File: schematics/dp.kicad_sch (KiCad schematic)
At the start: 27 parts, among them J9 DisplayPort_Molex_472720001, U28 74AVC4T245_UQFN, U29 FIN1019MTC, U30 TPD4E05U06QDQARQ1, U31 824012823

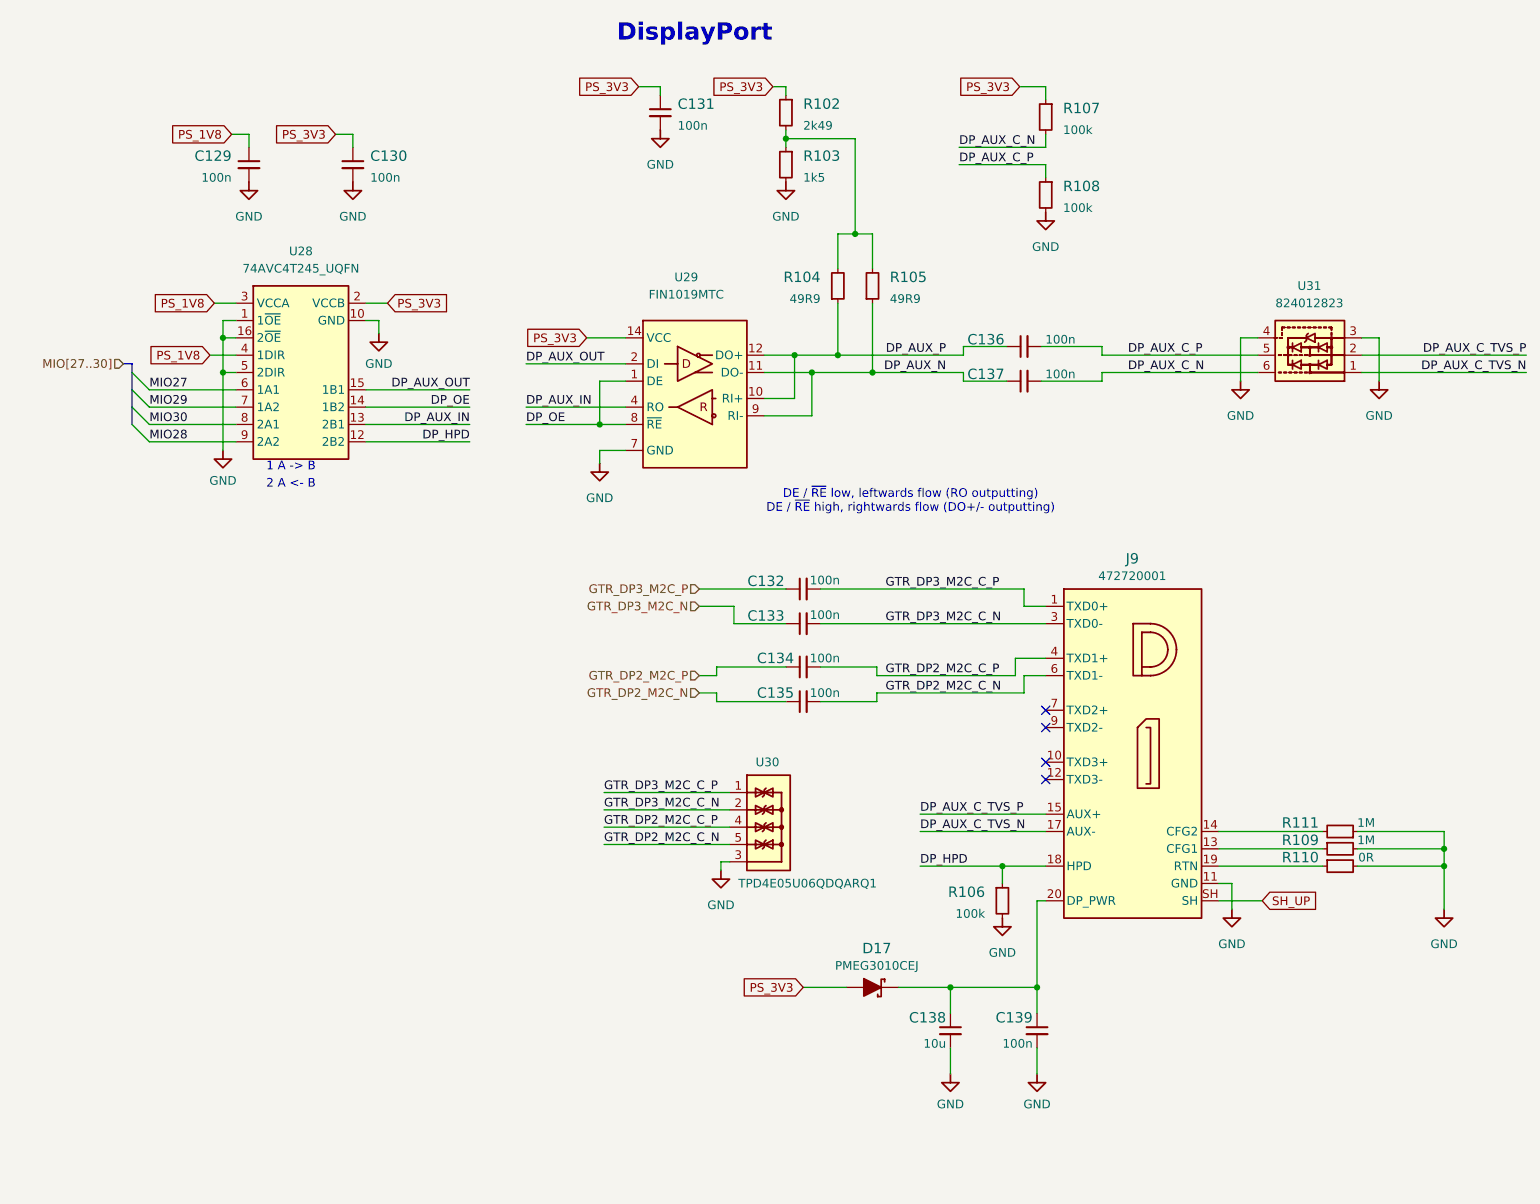
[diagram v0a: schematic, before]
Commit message: Voltage converter added
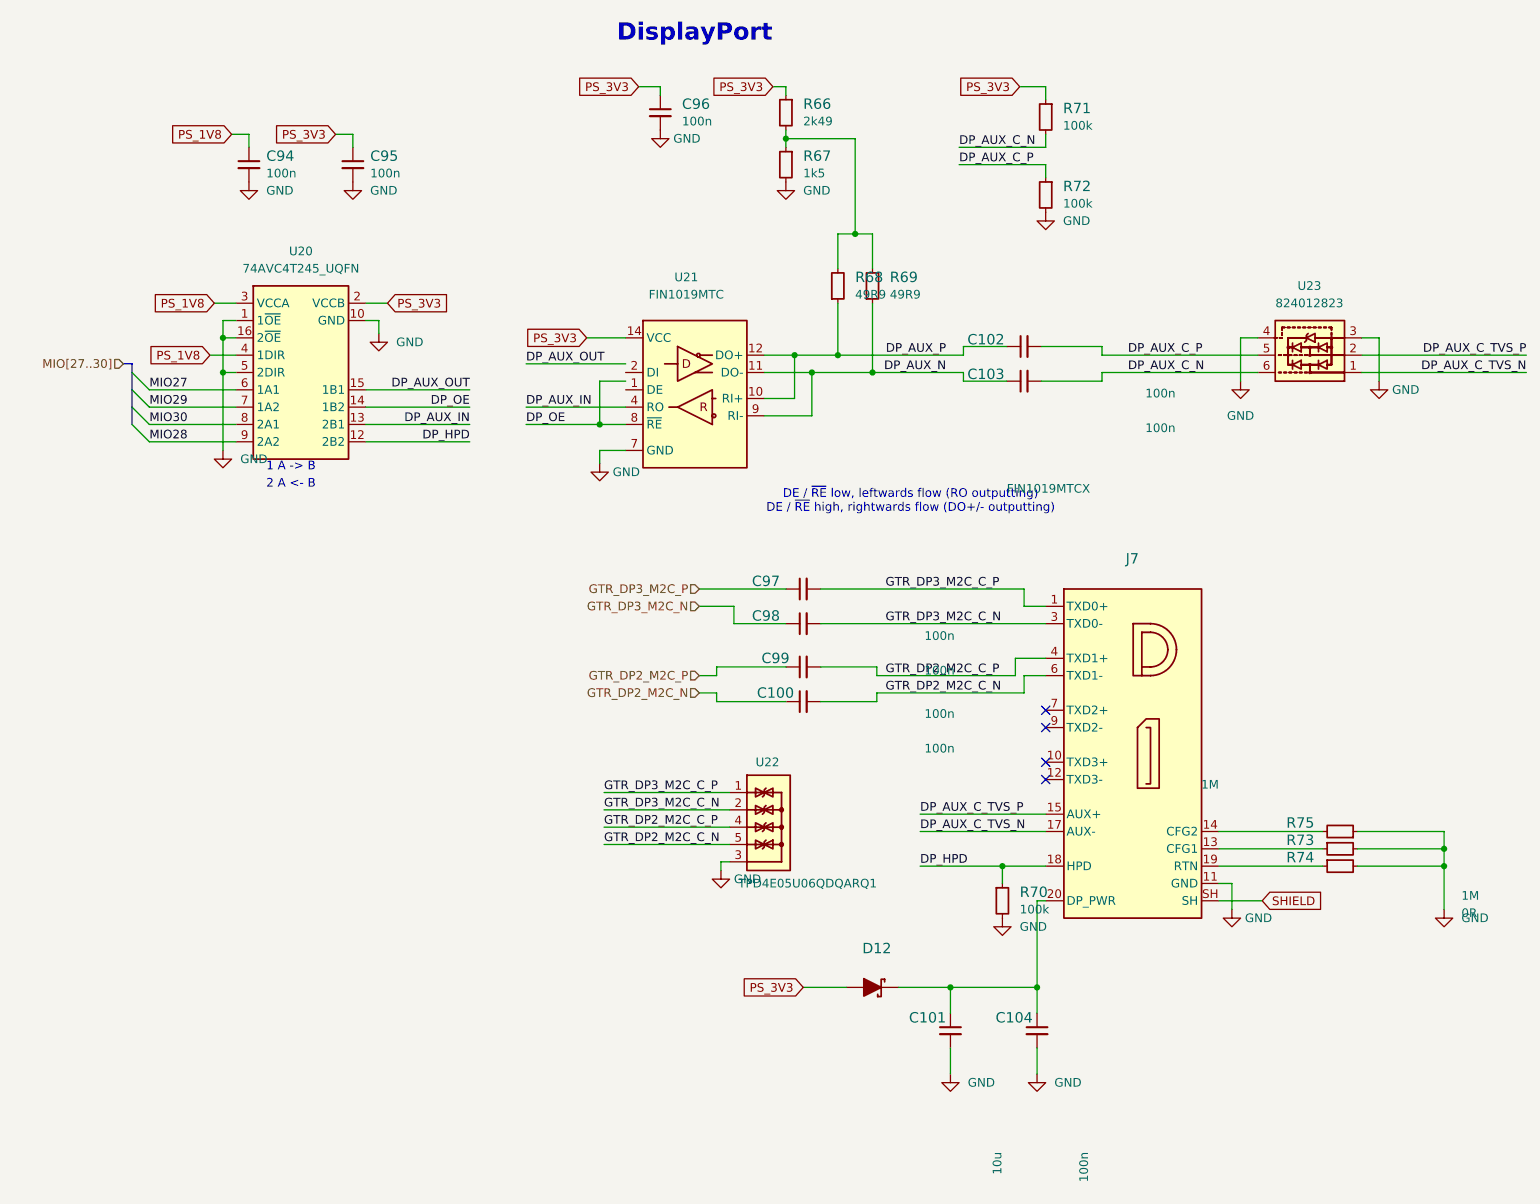
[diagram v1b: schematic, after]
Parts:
- C101: renamed from C138; Manufacturer Yaego -> YAGEO
- renumbered C135 to C100, C136 to C102, C137 to C103, C139 to C104, C129 to C94, C130 to C95, C131 to C96, C132 to C97, C133 to C98, C134 to C99, D17 to D12, J9 to J7, R102 to R66, R103 to R67, R104 to R68, R105 to R69, R106 to R70, R107 to R71, R108 to R72, R109 to R73, R110 to R74, R111 to R75, U28 to U20, U29 to U21, U30 to U22, U31 to U23
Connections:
- net DP_AUX_OUT: no longer U21.2 (DI)
- net DP_OE: no longer U21.1 (DE)
- net SH_UP renamed SHIELD
- now unconnected: U21.13 (NC), U21.3 (NC), U21.5 (NC), U21.6 (NC)
